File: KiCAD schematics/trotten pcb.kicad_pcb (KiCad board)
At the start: 2 copper layers, 22.9 x 22.9 mm, 10 parts, among them J1 Conn_01x04_Socket, J2 Conn_01x05_Socket, J3 Conn_01x05_Socket, J4 Conn_01x04_Socket, J5 Conn_02x03_Odd_Even, U1 S09-EY9-DC-DC, U2 BOB-12009, U3 ADAFRUIT-ESP32-S3, U7 INA260

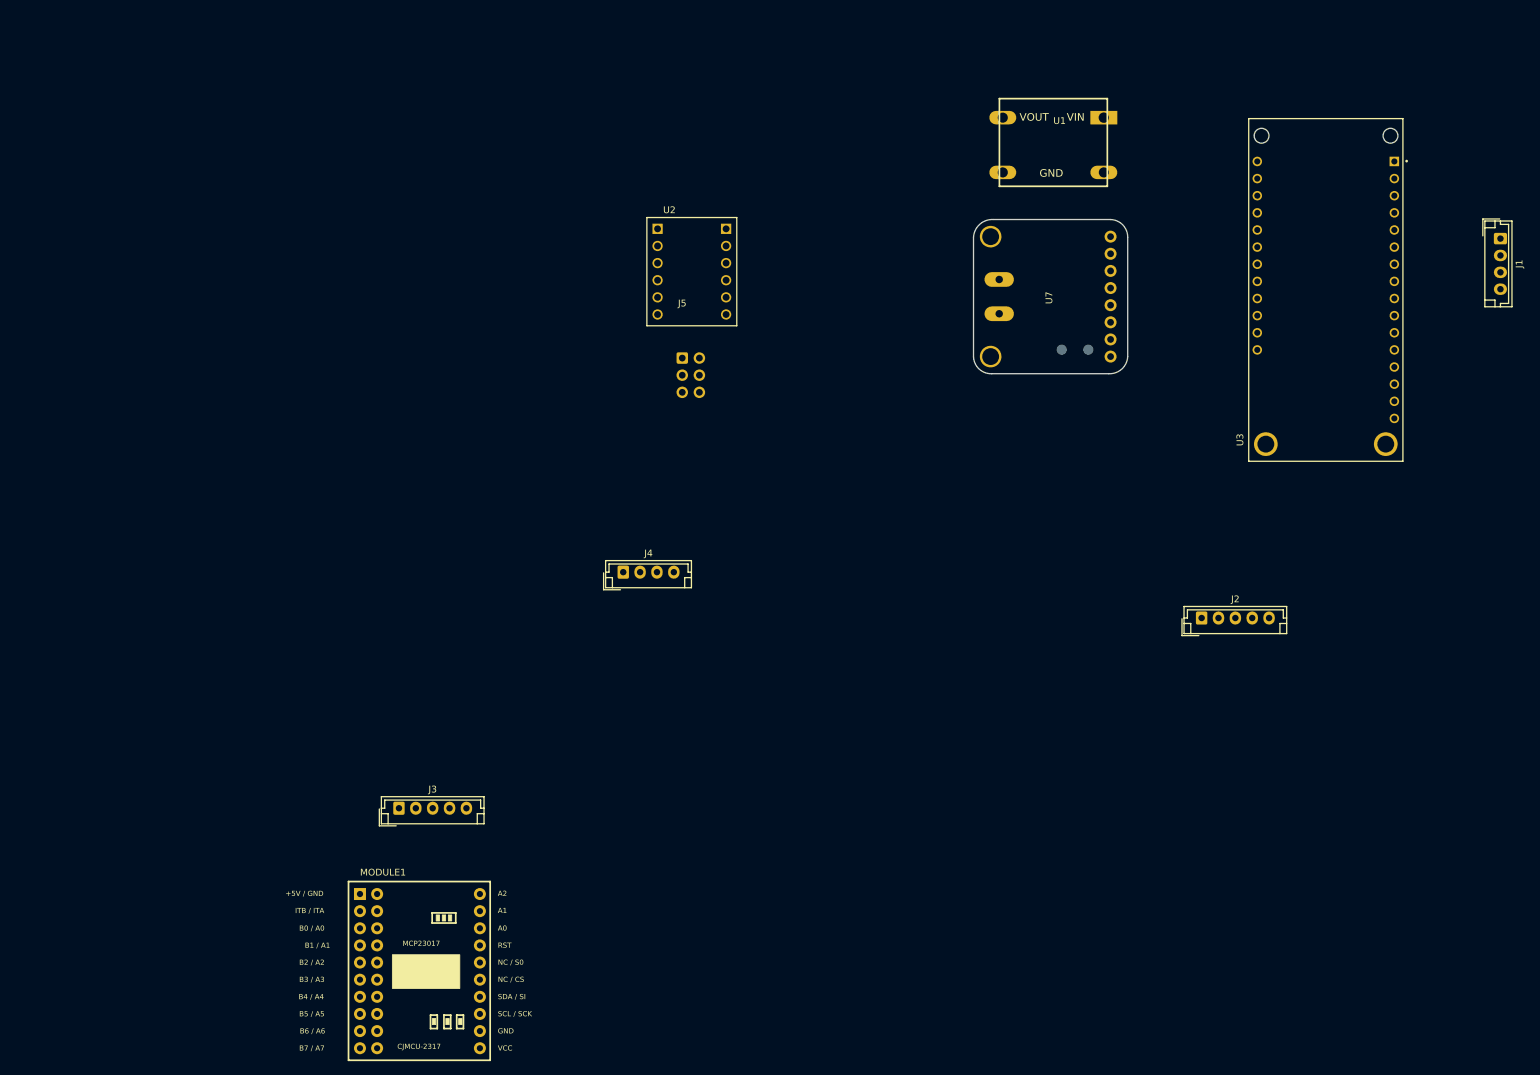
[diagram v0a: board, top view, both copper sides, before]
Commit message: SSD1306 working on esp32 s3
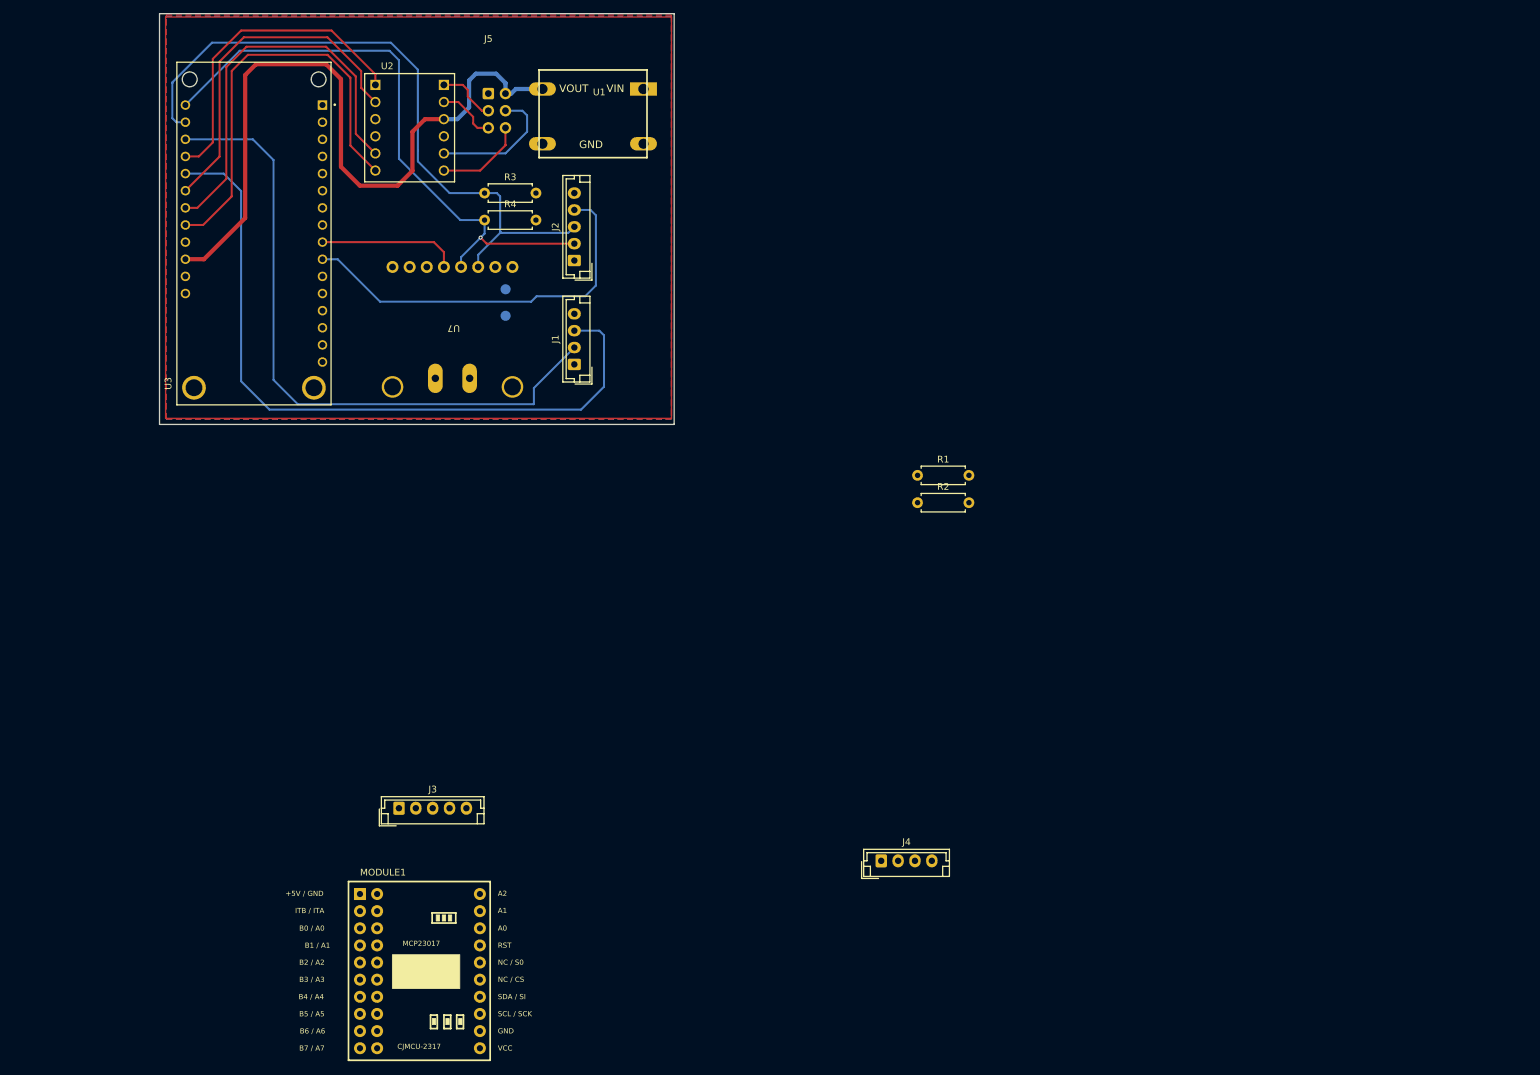
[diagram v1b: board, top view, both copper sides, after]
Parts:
- added R1: 10k, Resistor_THT:R_Axial_DIN0207_L6.3mm_D2.5mm_P7.62mm_Horizontal, F.Cu at (188.9, 92.3)
- added R2: 10k, Resistor_THT:R_Axial_DIN0207_L6.3mm_D2.5mm_P7.62mm_Horizontal, F.Cu at (188.9, 96.4)
- added R3: 10k, Resistor_THT:R_Axial_DIN0207_L6.3mm_D2.5mm_P7.62mm_Horizontal, F.Cu at (124.7, 50.5)
- added R4: 10k, Resistor_THT:R_Axial_DIN0207_L6.3mm_D2.5mm_P7.62mm_Horizontal, F.Cu at (124.7, 54.5)
- J1: value Conn_01x04_Socket -> Conn_HRCU4_main
- J2: value Conn_01x05_Socket -> Conn_screen_BRD_main
- J3: value Conn_01x05_Socket -> Conn_screen_BRD_Slave
- moved U3 159.1 mm to (90.5, 56.5)
- moved J1 138.6 mm to (138.0, 75.9), turned to 90 degrees
- moved J2 107.0 mm to (138.0, 60.5), turned to 90 degrees
- moved U1 68.4 mm to (140.8, 38.8)
- moved U7 65.6 mm to (131.5, 82.0), turned to 180 degrees
- moved J4 57.4 mm to (183.5, 149.5)
- moved J5 48.6 mm to (125.2, 28.1)
- moved U2 47.0 mm to (113.6, 40.8)
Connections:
- J2 pad 4: unconnected-(J2-Pin_4-Pad4) -> INT B - GP34
- U3 pad 10: unconnected-(U3-A2/IO34-Pad10) -> INT B - GP34
- U3 pad 9: unconnected-(U3-A3/IO39-Pad9) -> INT CUR - GP39
- U7 pad 7: unconnected-(U7-ALERT-Pad7) -> INT CUR - GP39
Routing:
- net +5V: track 0.00 -> 107.4 mm
- net ECHO - D15: track 0.00 -> 106.8 mm
- net SCL - GP22: track 0.00 -> 99.2 mm
- net TRIG - D14: track 0.00 -> 97.9 mm
- net SDA - GPI 23: track 0.00 -> 89.3 mm, vias 0 -> 1
- net R-PWM: track 0.00 -> 62.5 mm
- net R-EN: track 0.00 -> 59.3 mm
- net INT B - GP34: track 0.00 -> 58.1 mm
- net L-PWM: track 0.00 -> 51.3 mm
- net L-EN: track 0.00 -> 47.4 mm
- net INT CUR - GP39: track 0.00 -> 20.8 mm
- net Net-(J5-Pin_3): track 0.00 -> 19.6 mm
- net Net-(J5-Pin_1): track 0.00 -> 13.3 mm
- net Net-(J5-Pin_2): track 0.00 -> 8.76 mm
- net Net-(J5-Pin_4): track 0.00 -> 8.76 mm
- added copper zone on F.Cu, net +3.3V
- added copper zone on B.Cu, net GND
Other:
- board size 22.9 x 22.9 mm -> 76.3 x 60.9 mm

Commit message: avancement PCB et 3d files
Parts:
- added Brd1: SSD1306, SSD1306:SSD1306, F.Cu at (171.9, 127.4)
- added SW1: Haut, Button_6_6:6x6x5_Button, F.Cu at (93.2, 127.4)
- added SW2: Bas, Button_6_6:6x6x5_Button, F.Cu at (123.2, 127.4)
- added SW3: MEM_1, Button_6_6:6x6x5_Button, F.Cu at (65.8, 127.4)
- added SW4: MEM_2, Button_6_6:6x6x5_Button, F.Cu at (150.8, 127.4)
- J3, R1, R2: moved to B.Cu
- MODULE1: footprint CJMCU-2317 MCP23017 I2C SERIAL INTERFACE 16 BIT I:O EXPANDER SERIAL MODULE -> Adafruit_23017:MCP23017_ADAFRUIT; moved to B.Cu
- moved J3 42.9 mm to (74.2, 121.4)
- moved R1 38.8 mm to (188.2, 131.2), turned to 90 degrees
- moved R2 35.1 mm to (184.2, 131.2), turned to 90 degrees
- moved MODULE1 28.5 mm to (114.6, 127.2), turned to 180 degrees
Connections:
- MODULE1 pad 16: Net-(MODULE1-B3) -> unconnected-(MODULE1-B3-Pad16)
- MODULE1 pad 27: Net-(MODULE1-SDA/SI) -> Net-(Brd1-SDA)
- MODULE1 pad 28: Net-(MODULE1-SCL/SCK) -> Net-(Brd1-SCL)
- R1 pad 2: Net-(MODULE1-SCL/SCK) -> Net-(Brd1-SCL)
- R2 pad 2: Net-(MODULE1-SDA/SI) -> Net-(Brd1-SDA)
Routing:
- net Net-(Brd1-SCL): track 0.00 -> 131.8 mm
- net Net-(Brd1-SDA): track 0.00 -> 128.0 mm
- net +3.3V: track 0.00 -> 125.6 mm, vias 0 -> 1
- net Net-(MODULE1-B5): track 0.00 -> 59.7 mm
- net Net-(MODULE1-B6): track 0.00 -> 51.6 mm
- net Net-(J3-Pin_4): track 0.00 -> 49.7 mm, vias 0 -> 2
- net Net-(MODULE1-B4): track 0.00 -> 44.7 mm, vias 0 -> 1
- net Net-(MODULE1-B7): track 0.00 -> 36.1 mm
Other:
- board size 76.3 x 60.9 mm -> 151 x 114.3 mm

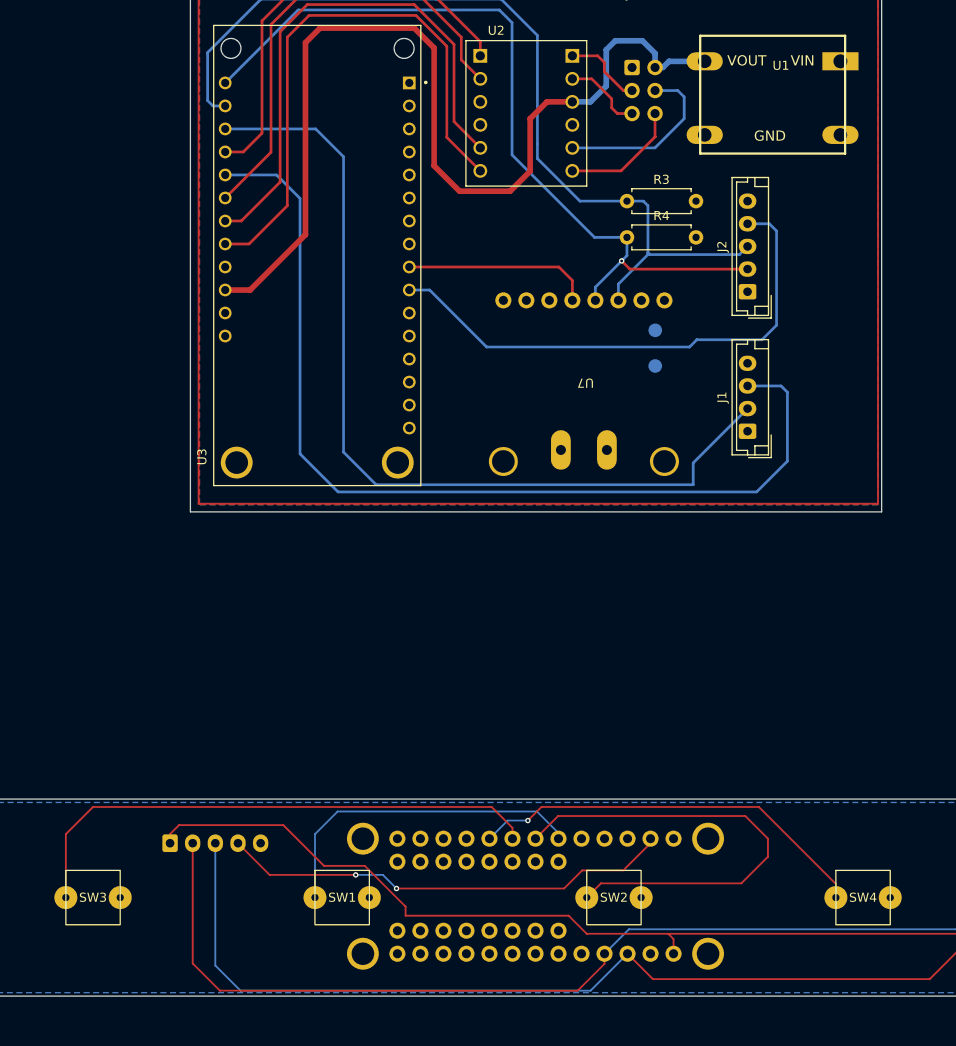
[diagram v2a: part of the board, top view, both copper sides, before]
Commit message: avancé INA260
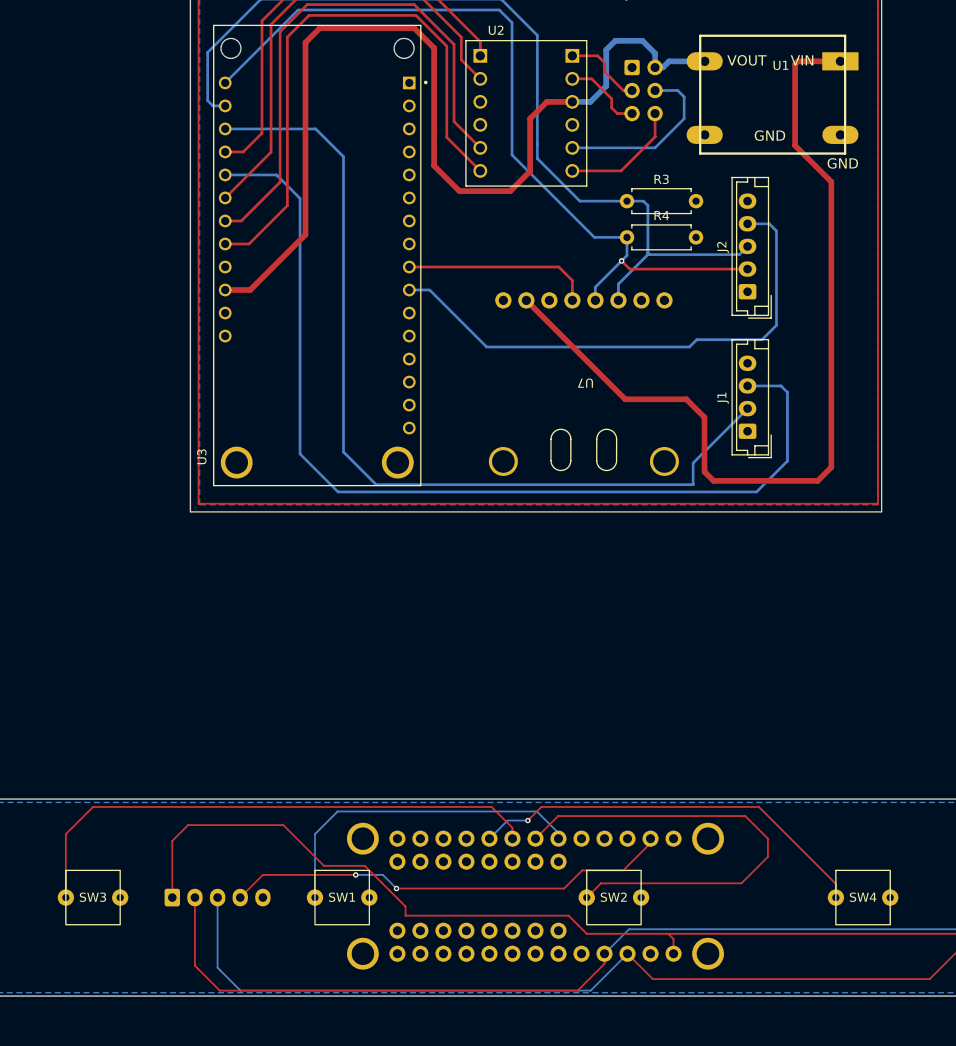
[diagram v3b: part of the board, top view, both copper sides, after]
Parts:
- U1: value S09-EY9-DC-DC -> std:8a282036eb974780bd16e9b19a8357be
- moved J3 6.01 mm to (74.5, 127.4)
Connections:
- U7 pad 10: +3.3V -> (no net)
- U7 pad 12: unconnected-(U7-VBUS-Pad12) -> (no net)
- U7 pad 14: Net-(U7-IN--Pad14) -> (no net)
- U7 pad 9: SCL - GP22 -> (no net)
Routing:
- net +12V: track 0.00 -> 97.3 mm
- net Net-(Brd1-SDA): track 128.0 -> 121.9 mm
- net Net-(Brd1-SCL): track 131.8 -> 125.7 mm
- net +3.3V: track 125.6 -> 130.9 mm
- net Net-(J3-Pin_4): track 49.7 -> 49.0 mm

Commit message: commencé le moteur
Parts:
- added J7: Screw_Terminal_01x04, TerminalBlock_Phoenix:TerminalBlock_Phoenix_MPT-0,5-4-2.54_1x04_P2.54mm_Horizontal, F.Cu at (130.2, 27.9)
- added REF**: MountingHole_2.2mm_M2, MountingHole:MountingHole_2.2mm_M2, F.Cu at (79.8, 26.9)
- added REF**: MountingHole_2.2mm_M2, MountingHole:MountingHole_2.2mm_M2, F.Cu at (149.8, 26.9)
- added REF**: MountingHole_2.2mm_M2, MountingHole:MountingHole_2.2mm_M2, F.Cu at (145.8, 76.4)
- U1: value std:8a282036eb974780bd16e9b19a8357be -> S09-EY9-DC-DC
- moved U1 0.62 mm to (140.8, 39.4)
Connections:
- U7 pad 1: +12V -> unconnected-(U7-IN+-Pad1)
- U7 pad 10: (no net) -> +3.3V
- U7 pad 12: (no net) -> unconnected-(U7-VBUS-Pad12)
- U7 pad 14: (no net) -> Net-(U7-IN--Pad14)
- U7 pad 9: (no net) -> SCL - GP22
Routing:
- net +12V: track 97.3 -> 26.5 mm
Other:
- outline, holes or cut-outs redrawn
- board text added: "12V"
- board text added: "GND"
- board text added: "HRC04 connector"
- board text added: "Screen connector"
